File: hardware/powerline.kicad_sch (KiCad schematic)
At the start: 2 parts, among them U1 ESP32-WROOM-32E

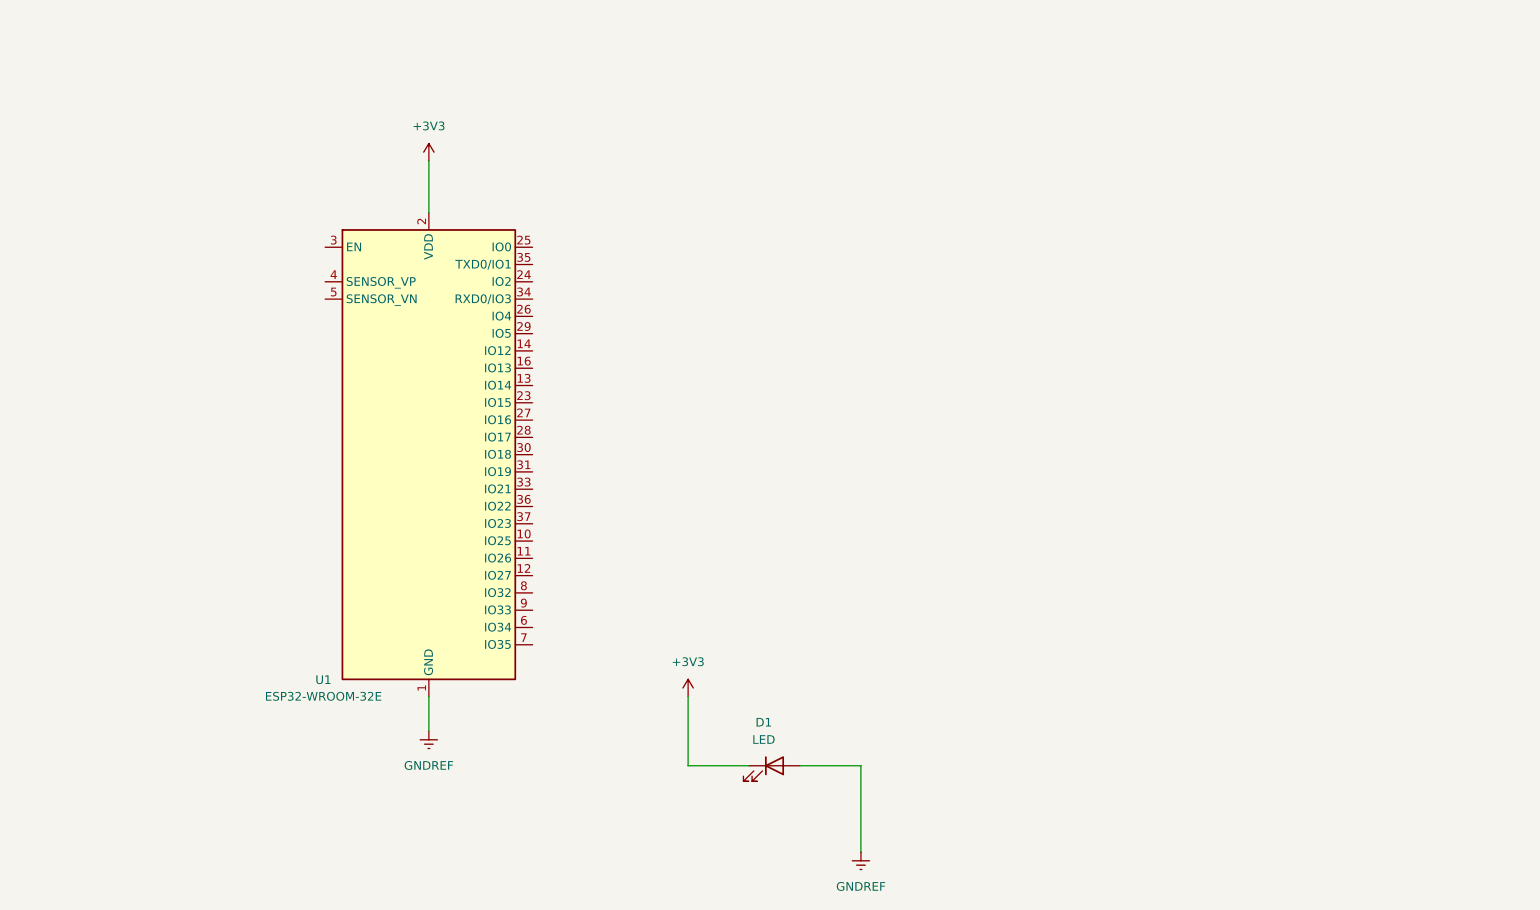
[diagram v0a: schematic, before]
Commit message: create schema for power section
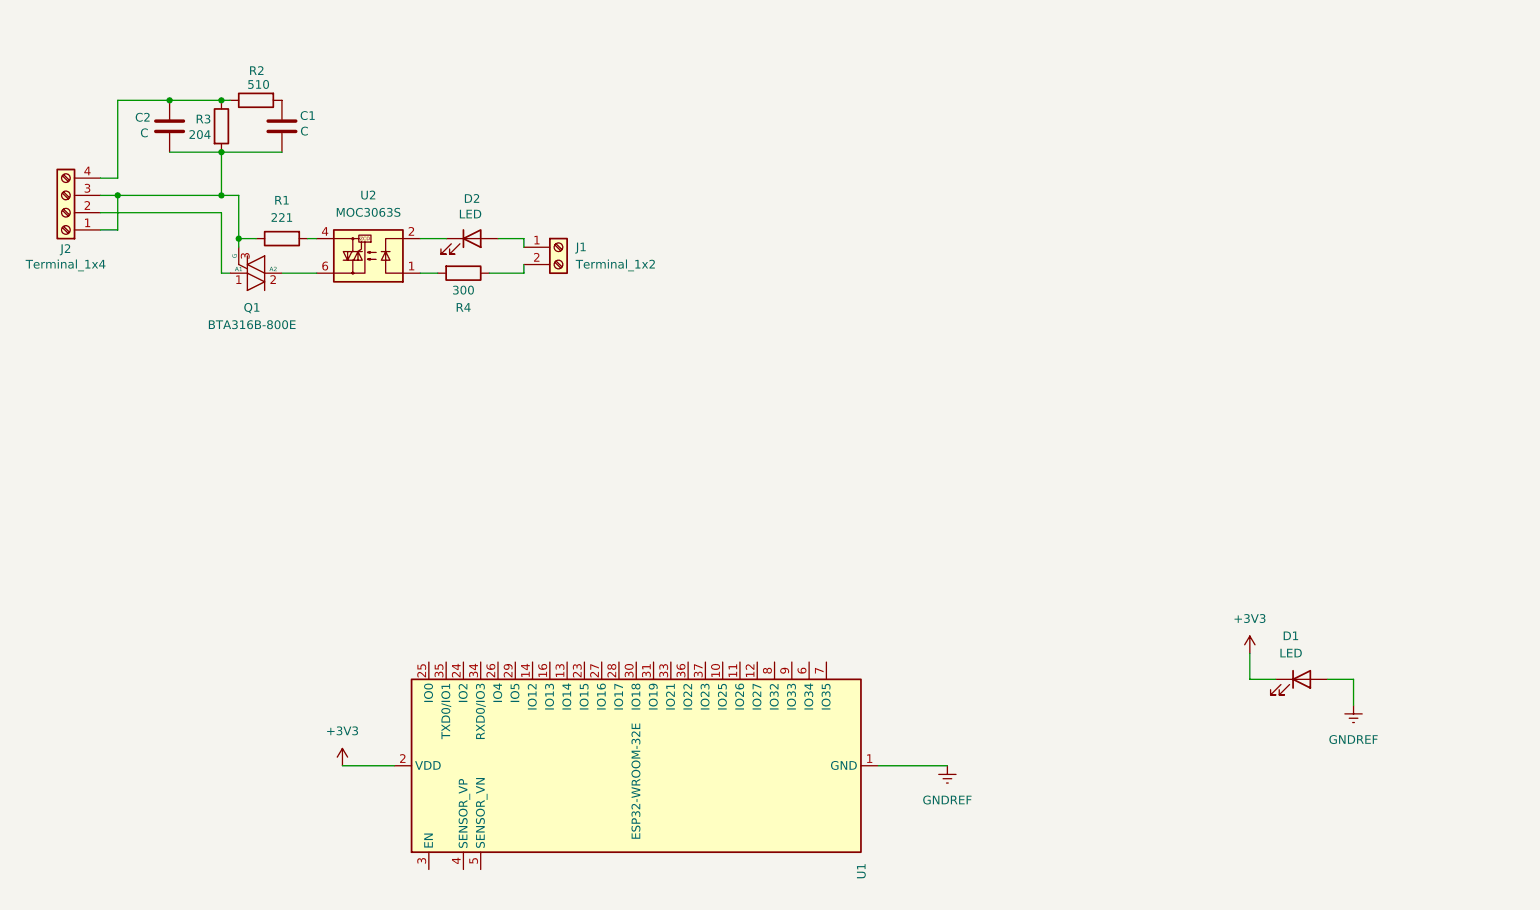
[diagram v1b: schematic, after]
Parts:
- added C1, C2: C, symbol Device:C
- added D2: LED, symbol Device:LED
- added J1: Terminal_1x2, symbol Connector:Screw_Terminal_01x02
- added J2: Terminal_1x4, symbol Connector:Screw_Terminal_01x04
- added Q1: BTA316B-800E, Package_TO_SOT_THT:TO-220-3_Vertical, symbol Triac_Thyristor:BTA16-800B
- added R1: 221, symbol Device:R
- added R2: 510, symbol Device:R
- added R3: 204, symbol Device:R
- added R4: 300, symbol Device:R
- added U2: MOC3063S, symbol Relay_SolidState:MOC3063M
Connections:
- new net: J2.2 (Pin_2), Q1.1 (A1)
- new net: Q1.2 (A2), U2.6
- new net: C1.2, C2.2, J2.1 (Pin_1), J2.3 (Pin_3), Q1.3 (G), R1.1, R3.2
- new net: D2.1 (K), U2.2
- new net: D2.2 (A), J1.1 (Pin_1)
- new net: C2.1, J2.4 (Pin_4), R2.1, R3.1
- new net: C1.1, R2.2
- new net: J1.2 (Pin_2), R4.1
- new net: R4.2, U2.1
- new net: R1.2, U2.4
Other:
- moved on the sheet: D1, U1

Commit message: add power feed
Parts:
- removed J2: Terminal_1x4, symbol Connector:Screw_Terminal_01x04
- added J3: Out_Terminal_1x2, symbol Connector:Screw_Terminal_01x02
- added PS1: HLK-10M03, Converter_ACDC:Converter_ACDC_Hi-Link_HLK-10Mxx, symbol Converter_ACDC:HLK-10M03
- J1: value Terminal_1x2 -> In_Terminal_1x2
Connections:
- net N: now reaches Q1.1 (A1)
- net N: now also C2.1, J1.1 (Pin_1), R2.1, R3.1, J3.1 (Pin_1), PS1.2 (AC/N)
- net L: now reaches C1.2, C2.2, Q1.3 (G), R1.1, R3.2
- net L: now also J1.2 (Pin_2), J3.2 (Pin_2), PS1.1 (AC/L)
- net at D2.2 (A): no longer J1.1 (Pin_1)
- net at R4.1: no longer J1.2 (Pin_2)
- net +3V3 renamed VCC
- net GNDREF renamed GND
- net GND: now also PS1.3 (-Vout); no longer D1.2 (A)
- new net: D1.2 (A), PS1.4 (+Vout)
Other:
- moved on the sheet: C1, C2, D1, D2, J1, Q1, R1, R2, R3, R4, U1, U2

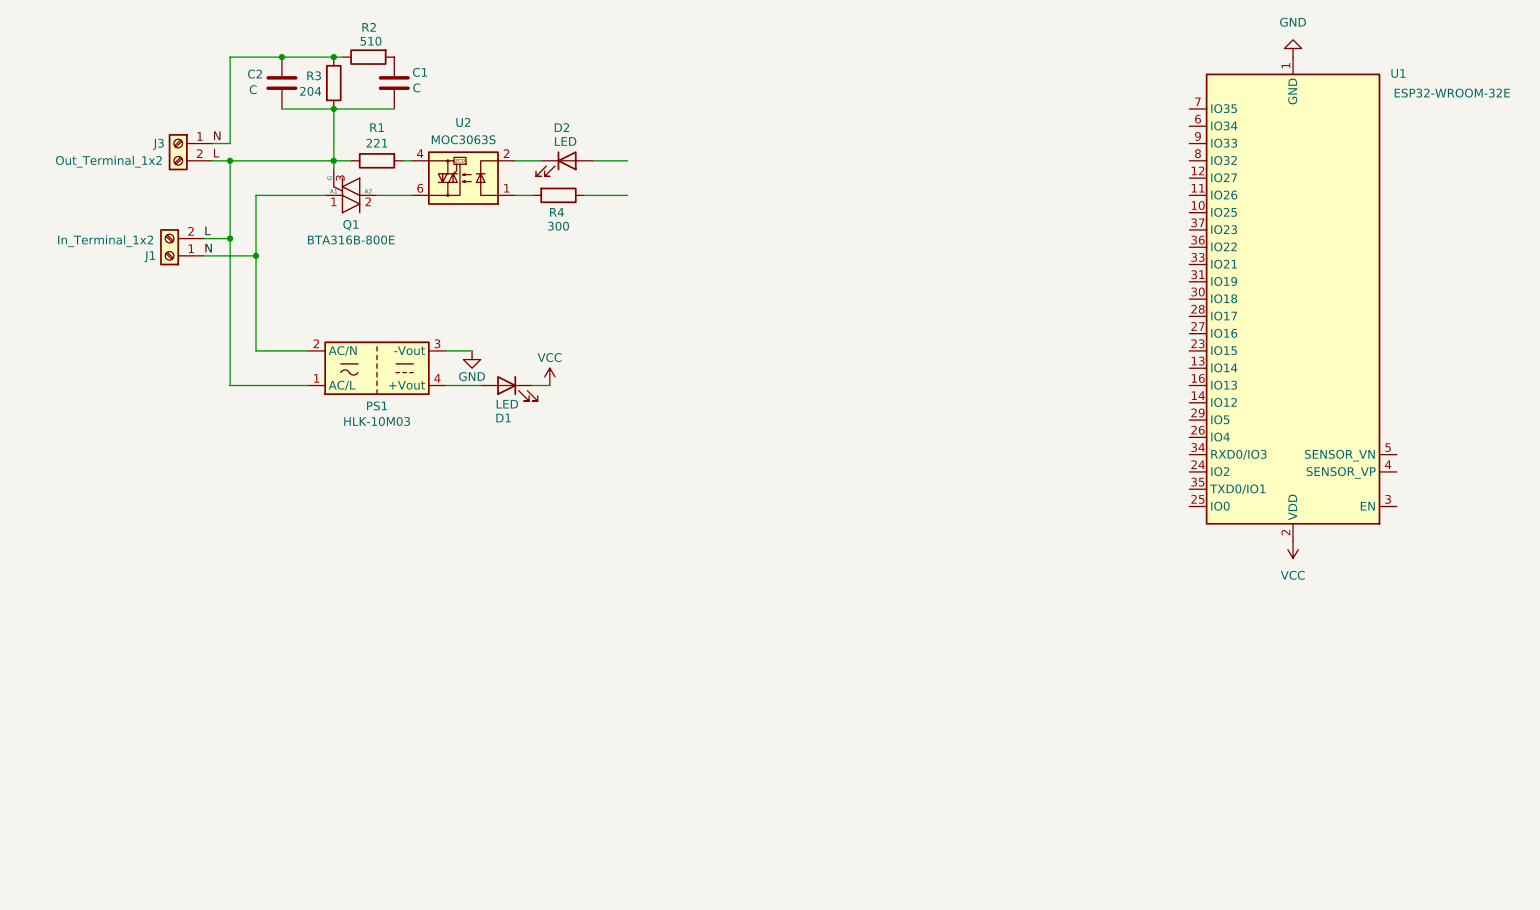
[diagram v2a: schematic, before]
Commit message: add led to power
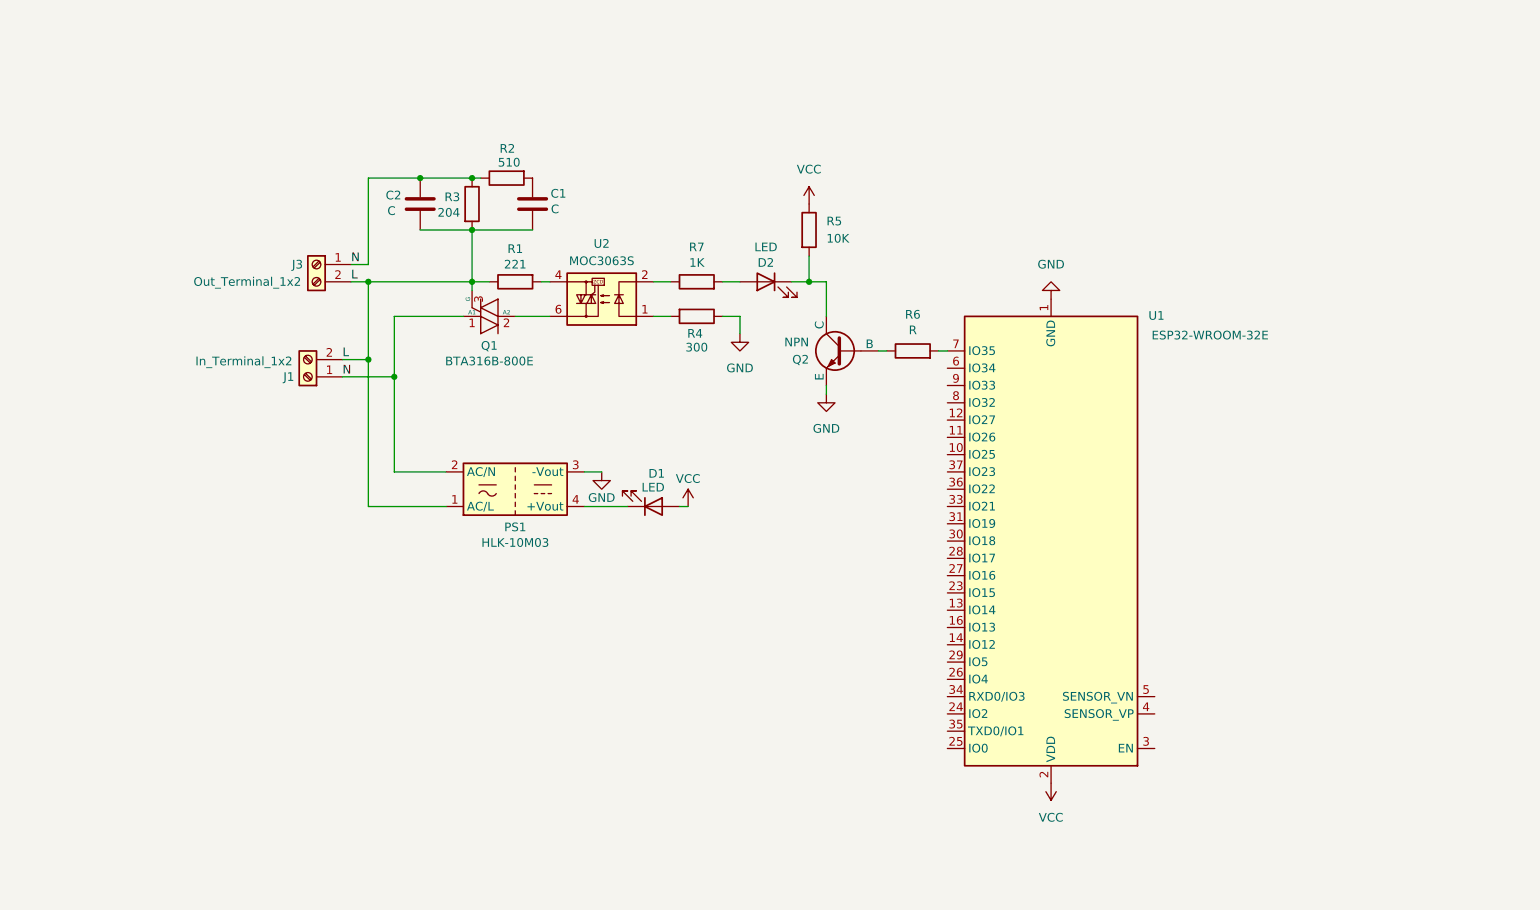
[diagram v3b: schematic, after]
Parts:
- added Q2: NPN, symbol Simulation_SPICE:NPN
- added R5: 10K, symbol Device:R
- added R6: R, symbol Device:R
- added R7: 1K, symbol Device:R
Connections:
- net GND: now also R4.1, Q2.3 (E)
- net VCC: now also D1.2 (A), R5.1; no longer D1.1 (K)
- net at D2.1 (K): now also Q2.1 (C), R5.2; no longer U2.2
- net at D2.2 (A): now also R7.2
- net at PS1.4 (+Vout): now also D1.1 (K); no longer D1.2 (A)
- net at U1.7 (IO35): now also R6.2
- new net: R7.1, U2.2
- new net: Q2.2 (B), R6.1
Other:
- moved on the sheet: C1, C2, D1, D2, J1, J3, PS1, Q1, R1, R2, R3, R4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

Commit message: upgrade schema and pcb
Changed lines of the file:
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@@
 (kicad_sch
-	(version 20231120)
+	(version 20250114)
 	(generator "eeschema")
-	(generator_version "8.0")
+	(generator_version "9.0")
 	(paper "A4")
 	(title_block
@@
 		)
 	)
+	(embedded_fonts no)
 )
